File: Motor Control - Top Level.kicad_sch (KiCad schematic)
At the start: 0 parts

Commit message: [01/07/2026][MCU - IOs] Update
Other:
- company: (none) -> ${COMPANY}
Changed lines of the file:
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@@
 	(generator_version "9.0")
 	(paper "A4")
+	(title_block
+		(date "2026-06-27")
+		(company "${COMPANY}")
+	)
 )

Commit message: Update Power Connector & Motor Control Schematic
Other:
- added sheet Motor Control - Index (Motor Control - Index.kicad_sch)
- added sheet Motor Control - Middle (Motor Control - Middle.kicad_sch)
- added sheet Motor Control - Pinky (Motor Control - Pinky.kicad_sch)
- added sheet Motor Control - Ring (Motor Control - Ring.kicad_sch)
- added sheet Motor Control - Thumb 1 (Motor Control - Thumb 1.kicad_sch)
- added sheet Motor Control - Thumb 2 (Motor Control - Thumb 2.kicad_sch)

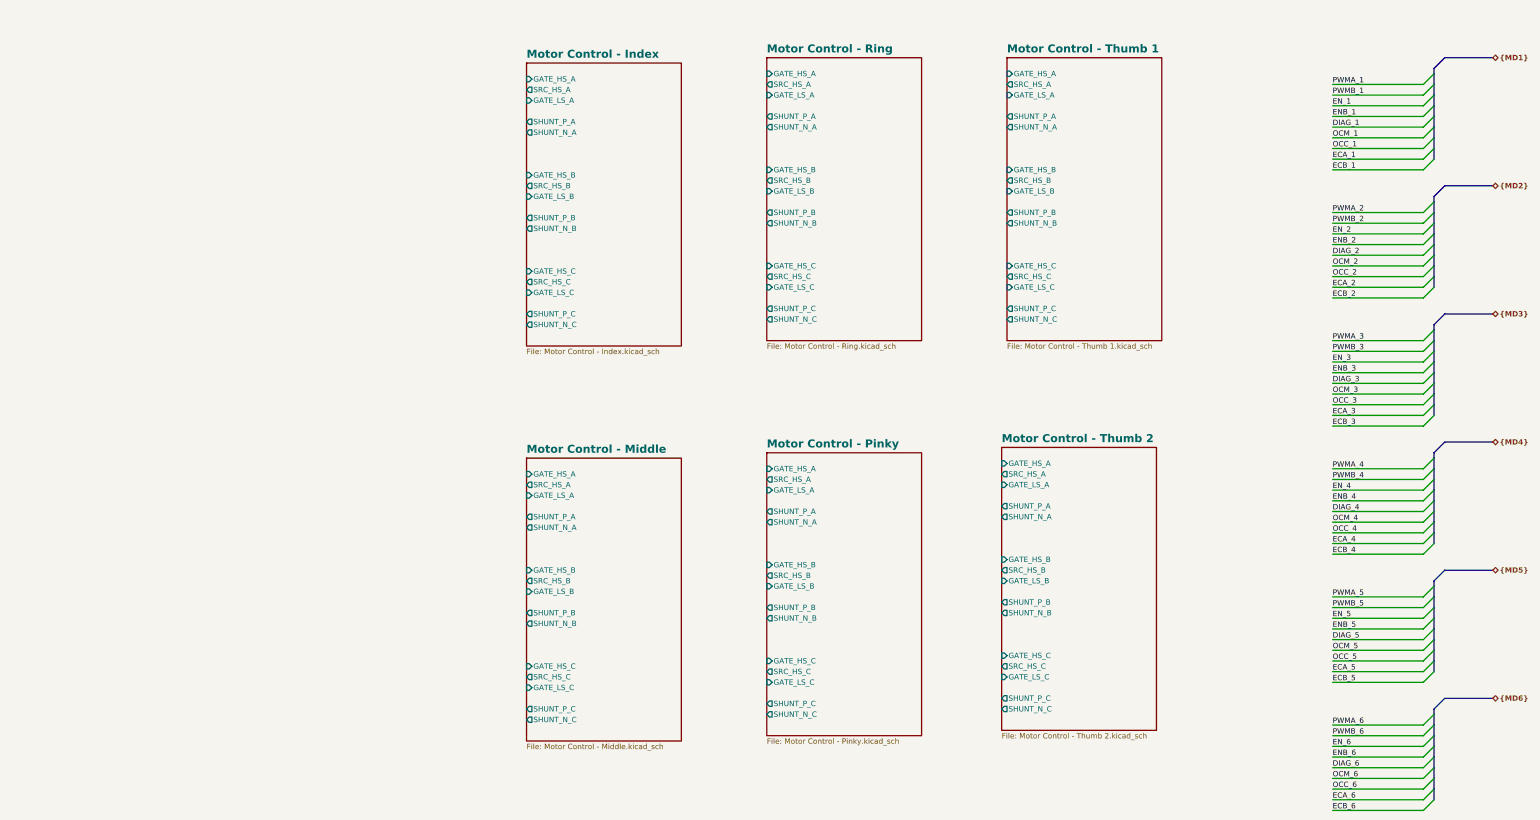
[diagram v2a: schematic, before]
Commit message: Update Motor Schematic
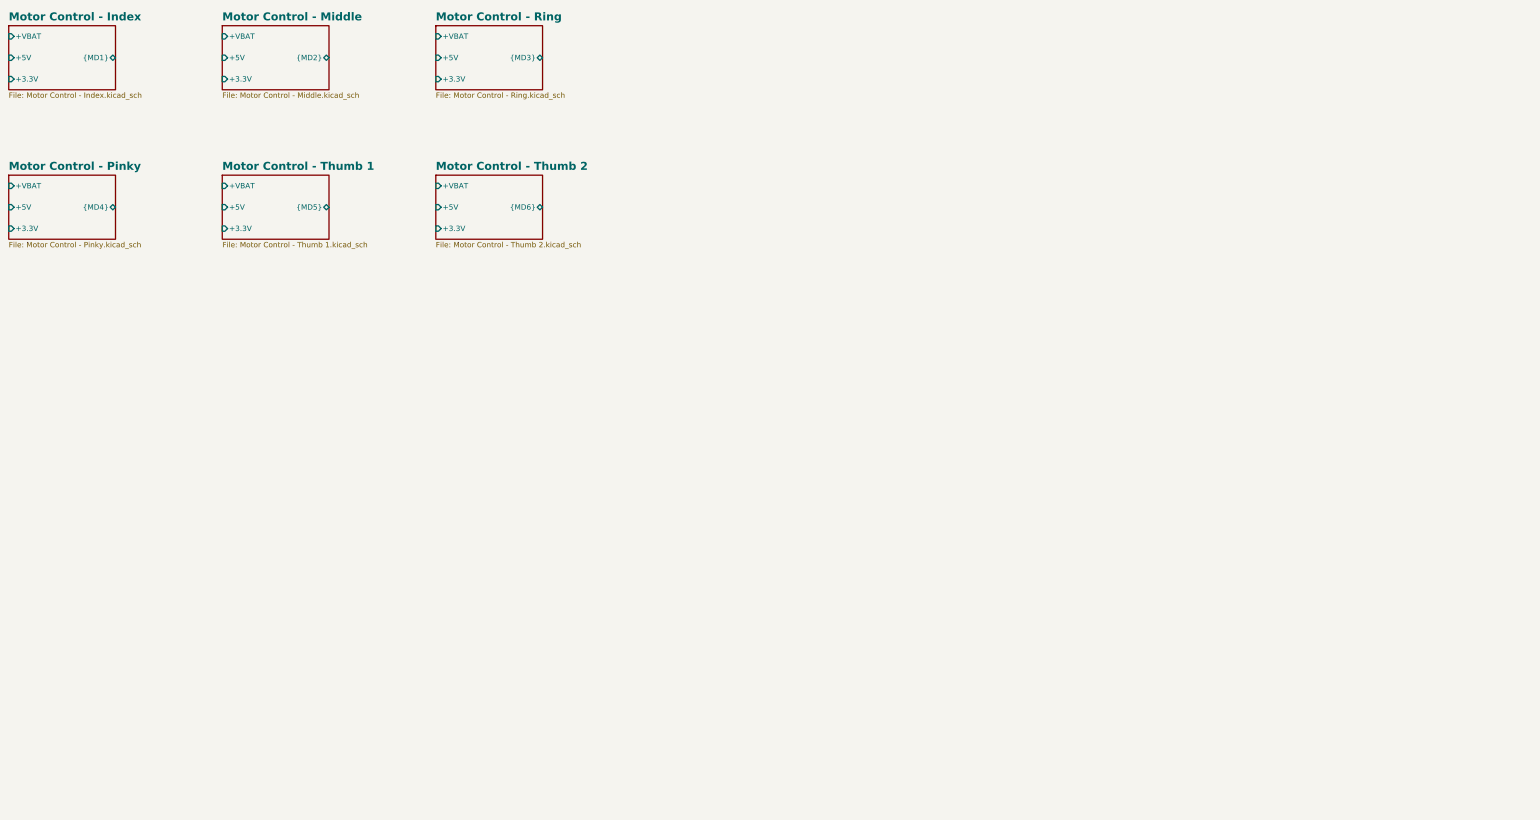
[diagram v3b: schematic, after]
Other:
- sheet Motor Control - Index ports: added +3.3V, +5V, +VBAT, {MD1}; removed GATE_HS_A, GATE_HS_B, GATE_HS_C, GATE_LS_A, GATE_LS_B, GATE_LS_C, SHUNT_N_A, SHUNT_N_B, SHUNT_N_C, SHUNT_P_A, SHUNT_P_B, SHUNT_P_C, SRC_HS_A, SRC_HS_B, SRC_HS_C
- sheet Motor Control - Middle ports: added +3.3V, +5V, +VBAT, {MD2}; removed GATE_HS_A, GATE_HS_B, GATE_HS_C, GATE_LS_A, GATE_LS_B, GATE_LS_C, SHUNT_N_A, SHUNT_N_B, SHUNT_N_C, SHUNT_P_A, SHUNT_P_B, SHUNT_P_C, SRC_HS_A, SRC_HS_B, SRC_HS_C
- sheet Motor Control - Pinky ports: added +3.3V, +5V, +VBAT, {MD4}; removed GATE_HS_A, GATE_HS_B, GATE_HS_C, GATE_LS_A, GATE_LS_B, GATE_LS_C, SHUNT_N_A, SHUNT_N_B, SHUNT_N_C, SHUNT_P_A, SHUNT_P_B, SHUNT_P_C, SRC_HS_A, SRC_HS_B, SRC_HS_C
- sheet Motor Control - Ring ports: added +3.3V, +5V, +VBAT, {MD3}; removed GATE_HS_A, GATE_HS_B, GATE_HS_C, GATE_LS_A, GATE_LS_B, GATE_LS_C, SHUNT_N_A, SHUNT_N_B, SHUNT_N_C, SHUNT_P_A, SHUNT_P_B, SHUNT_P_C, SRC_HS_A, SRC_HS_B, SRC_HS_C
- sheet Motor Control - Thumb 1 ports: added +3.3V, +5V, +VBAT, {MD5}; removed GATE_HS_A, GATE_HS_B, GATE_HS_C, GATE_LS_A, GATE_LS_B, GATE_LS_C, SHUNT_N_A, SHUNT_N_B, SHUNT_N_C, SHUNT_P_A, SHUNT_P_B, SHUNT_P_C, SRC_HS_A, SRC_HS_B, SRC_HS_C
- sheet Motor Control - Thumb 2 ports: added +3.3V, +5V, +VBAT, {MD6}; removed GATE_HS_A, GATE_HS_B, GATE_HS_C, GATE_LS_A, GATE_LS_B, GATE_LS_C, SHUNT_N_A, SHUNT_N_B, SHUNT_N_C, SHUNT_P_A, SHUNT_P_B, SHUNT_P_C, SRC_HS_A, SRC_HS_B, SRC_HS_C
